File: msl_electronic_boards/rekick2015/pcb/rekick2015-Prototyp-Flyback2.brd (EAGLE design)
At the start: 160 x 100 mm, 207 parts, among them IC1 74LVC1G02GW, IC2 4043D, IC3 LM1117, IC4 LM1458D, Q1 16MHz, Q2 IGW60T120, Q3 PSMN7R8-120PS, Q4 PSMN7R8-120PS, Q5 IPD90P04P4L, Q6 IRF840, T1 BC859, T2 BC849, T3 BC849, T4 BC849, T5 IRLML6344TRPBF, U1 TXB0108PWR, U3 LM2675, U4 LM2675, U5 ADUM4190BRIZ, U6 ADUM4190BRIZ

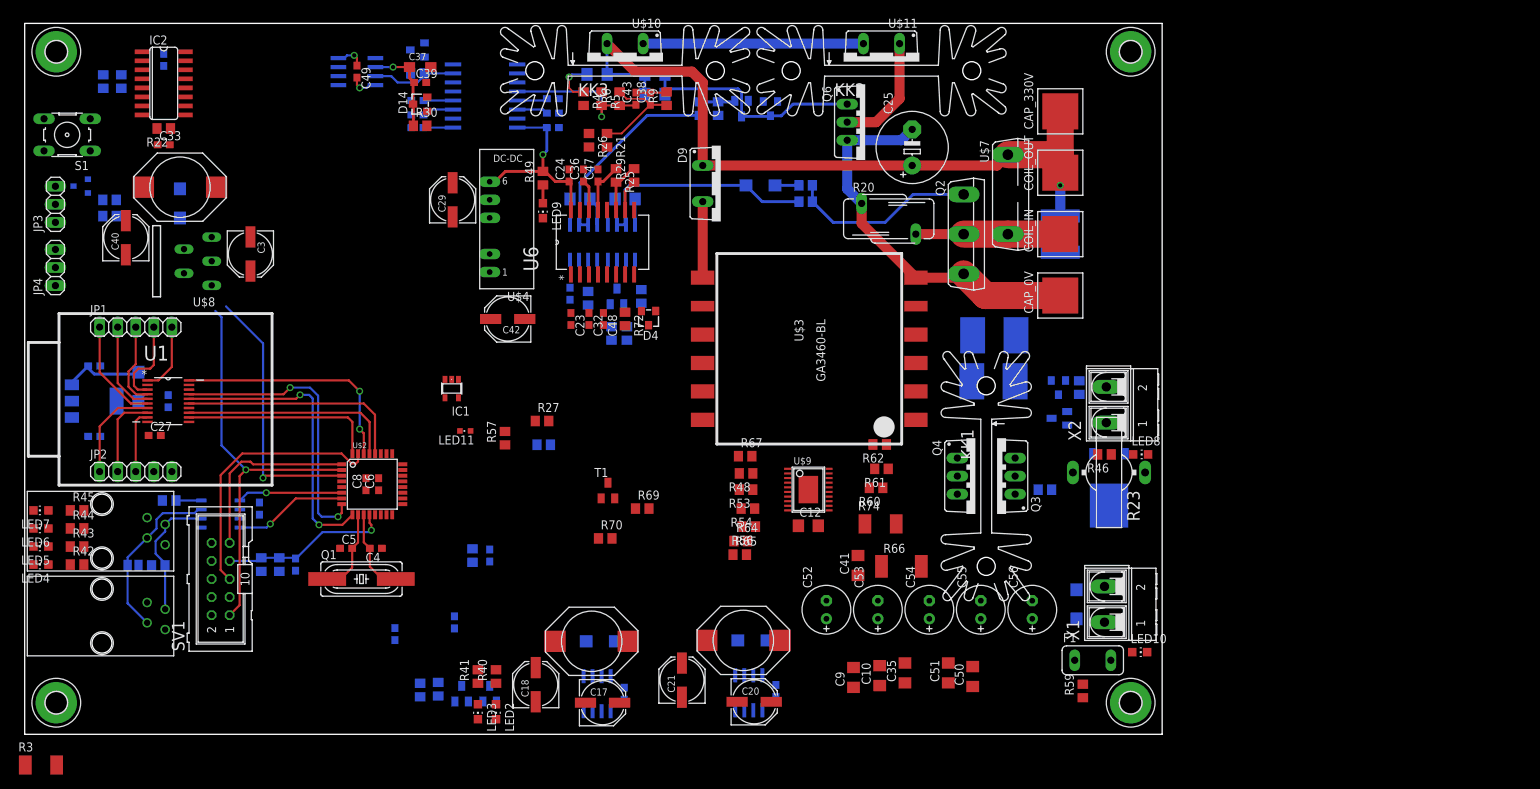
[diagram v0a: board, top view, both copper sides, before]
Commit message: rekick flyback layout
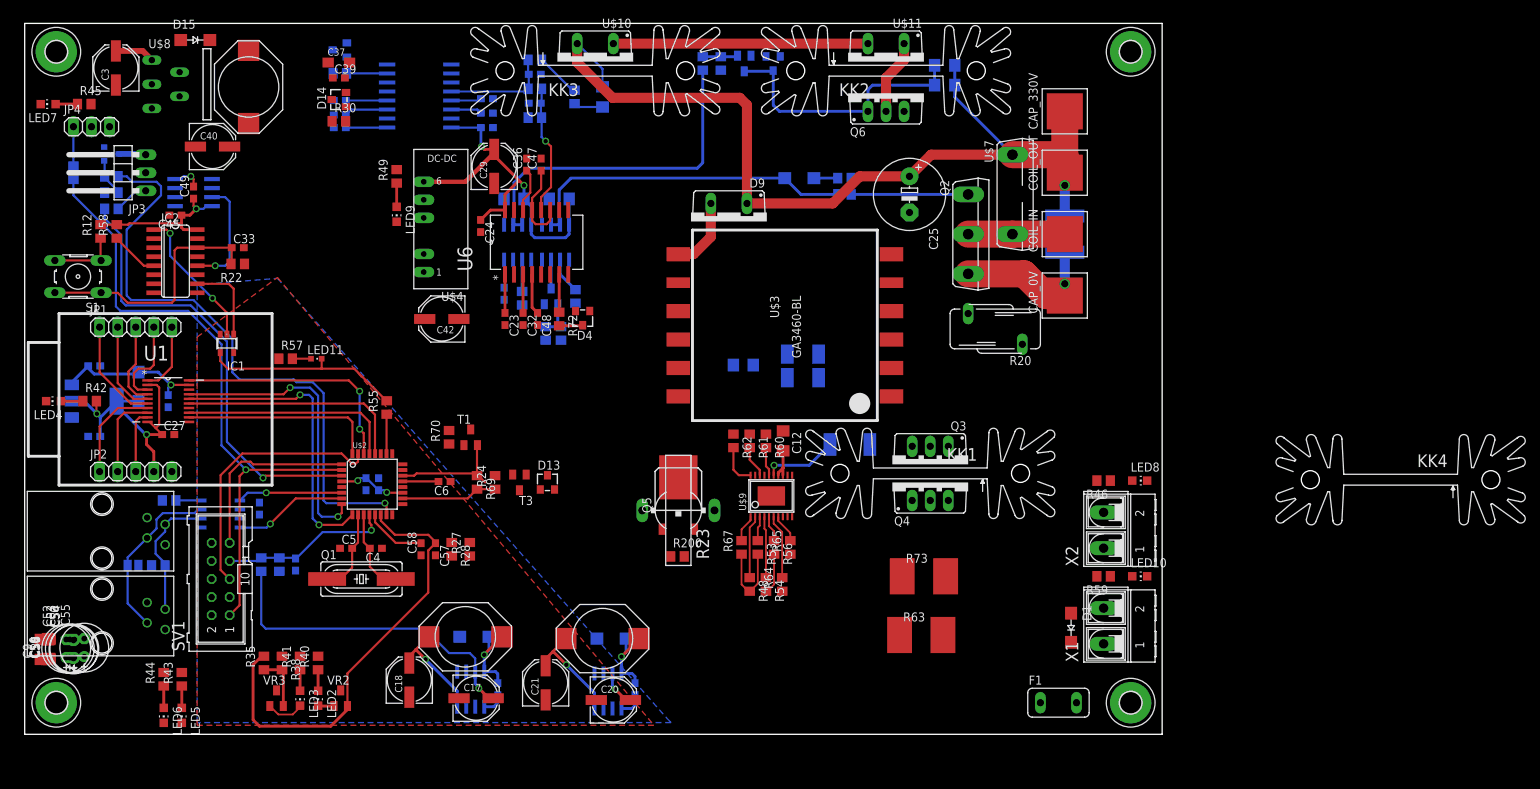
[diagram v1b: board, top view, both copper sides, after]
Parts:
- removed R21, R25: 1k, rcl:R0805
- removed R26, R29: 100k, rcl:R0805
- added KK4: SK104, heatsink:SK104
- added R7, R8: 5,6k, rcl:R0805
- JP3: device pinhead:1X03 -> pinhead:1X03/90
- R61, R67: value 40.2k -> 80.6k
- R62: value 18.2k -> 36.5k
- R69: value 50k -> 10k
- moved C56 135.0 mm to (6.86, 11.9)
- moved C50 130.0 mm to (3.43, 11.9)
- moved C51 126.7 mm to (3.30, 11.9)
- moved C55 126.2 mm to (8.38, 12.2)
- moved C35 120.4 mm to (3.43, 12.1)
- moved C54 120.4 mm to (6.99, 12.1)
- moved R3 120.2 mm to (109.5, 50.2), flipped to the bottom, turned to 180 degrees
- moved C10 117.2 mm to (3.17, 11.9)
- moved C9 114.4 mm to (2.29, 11.9)
- moved C53 113.8 mm to (6.35, 12.1)
- moved C52 107.1 mm to (5.84, 12.1)
- moved R24 77.3 mm to (66.2, 35.4), flipped to the top, turned to 90 degrees
- moved T3 76.5 mm to (69.6, 35.4), flipped to the top, turned to 180 degrees
- moved D13 73.1 mm to (73.5, 35.4), flipped to the top, turned to 0 degrees
- moved R200 61.3 mm to (91.8, 25.0), flipped to the top, turned to 0 degrees
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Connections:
- removed net N$51: R55.1, U$2.22
- removed net N$82: R21.2, R26.2, U6.12
- removed net N$83: R29.1, U6.10
- removed net N$84: C47.1, R25.1, U6.13
- new net N$12: JP4.1, R8.2
- new net N$13: R55.1, U$2.26
- new net N$2: JP3.1, R7.2
- net !FAULT: now also U$2.17; no longer U$2.18
- net +5V: now also C7.2, U$2.19
- net +5V/3: now also IC4.6; no longer C7.2, IC4.2, U$2.19
- net ACTIVATE_BOOSTER: now also U$2.18; no longer U$2.26
- net ADC_CAP_OV: now also IC4.5; no longer IC4.3
- net CAP_0V: now also H2.B3,0; no longer H1.B3,0, R26.1, R38.1, VR2.3, VR3.3
- net CHARGE: now also U$2.22; no longer U$2.17
- net GND: now also H1.B3,0, R38.1, VR2.3, VR3.3; no longer H2.B3,0
- net N$27: now also U6.12; no longer R21.1
- net N$85: now also C47.1, U6.13; no longer R25.2, R29.2
- net OC0A/MOSI_A: now also R8.1; no longer JP4.1
- net SERVO_PWM: now also R7.1; no longer JP3.1
- net ÜBERSPANNUNG: now also IC4.7; no longer IC4.1
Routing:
- net ACTIVATE_SERVO: track 0.00 -> 85.7 mm, vias 0 -> 1
- net ADC_CAP: track 0.00 -> 62.8 mm
- net +24V: track 0.00 -> 57.3 mm, vias 0 -> 2
- net +5V: track 15.4 -> 68.1 mm, vias 1 -> 5
- net +3V3: track 0.00 -> 40.6 mm, vias 0 -> 2
- net CAP_0V: track 59.3 -> 20.9 mm, vias 0 -> 1
- net TASTER: track 0.00 -> 35.1 mm
- net +12V: track 4.15 -> 37.2 mm, vias 0 -> 1
- net OC0A/MOSI_A: track 59.0 -> 91.4 mm
- net NOTAUS: track 0.00 -> 28.3 mm
- net SERVO_PWM: track 37.5 -> 63.6 mm
- net CAP_330V: track 105.5 -> 128.6 mm
- net N$38: track 0.00 -> 20.0 mm, vias 0 -> 2
- net N$41: track 28.1 -> 48.0 mm
- net CAP_+12V: track 34.7 -> 54.2 mm, vias 1 -> 2
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- added copper zone on layer 1, net GND
- added copper zone on layer 16, net GND
